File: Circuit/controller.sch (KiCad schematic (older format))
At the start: 13 parts, among them SW2 ROTARY_ENCODER_SWITCH, SW4 A, SW6 B, U4 JOYSTICK_W_BUTTON

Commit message: Rotated joystick to fit better.  X and Y are swapped.
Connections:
- net JOY_X: now also U4.Y2 (Y_WIPER); no longer U4.X2 (X_WIPER)
- net JOY_Y: now also U4.X2 (X_WIPER); no longer U4.Y2 (Y_WIPER)
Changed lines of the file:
@@
 Text HLabel 1000 850  2    60   Input ~ 0
 JOY_BUTTON
+Text HLabel 2500 1450 2    60   Input ~ 0
+JOY_X
 Text HLabel 2100 900  2    60   Input ~ 0
-JOY_X
-Text HLabel 2500 1450 2    60   Input ~ 0
 JOY_Y
 Wire Wire Line

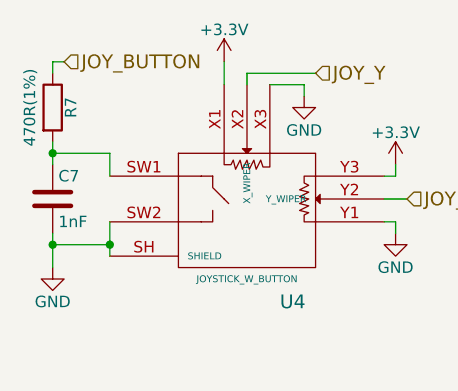
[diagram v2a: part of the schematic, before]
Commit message: More BOM - passives mostly.
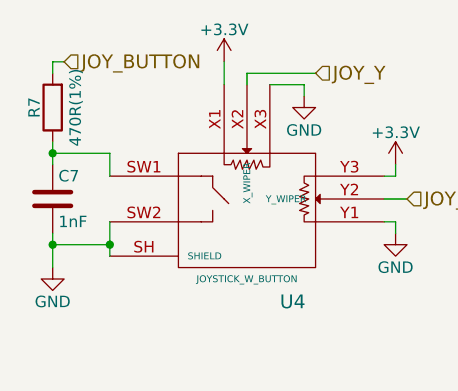
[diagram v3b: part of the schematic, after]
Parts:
- R10, R11, R8: Digikey PN (none) -> 311-10KGRCT-ND; Link (none) -> http://www.digikey.com.au/product-detail/en/yageo/RC0603JR-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; Manufacturer PN (none) -> RC0603JR-0710KL; Unit Cost (none) -> 0.10
- R12, R14, R7: Digikey PN (none) -> 311-470HRCT-ND; Link (none) -> http://www.digikey.com.au/product-detail/en/yageo/RC0603FR-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; Manufacturer PN (none) -> RC0603FR-07470RL; Unit Cost (none) -> 0.10
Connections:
- net JOY_BUTTON: now also R7.2; no longer R7.1
- net at C7.1, U4.SW1: now also R7.1; no longer R7.2
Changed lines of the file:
@@
-$EndComp
-$Comp
-L R R7
-U 1 1 58137E6F
-P 950 1050
-F 0 "R7" V 1030 1050 50  0000 C CNN
-F 1 "470R(1%)" V 850 1050 50  0000 C CNN
-F 2 "Resistors_SMD:R_0603_HandSoldering" V 880 1050 50  0001 C CNN
-F 3 "" H 950 1050 50  0000 C CNN
-	1    950  1050
-	1    0    0    -1
 $EndComp
 $Comp
@@
 $EndComp
 $Comp
-L R R12
-U 1 1 5813BFFC
-P 5450 1000
-F 0 "R12" V 5530 1000 50  0000 C CNN
-F 1 "470R(1%)" V 5350 1000 50  0000 C CNN
-F 2 "Resistors_SMD:R_0603_HandSoldering" V 5380 1000 50  0001 C CNN
-F 3 "" H 5450 1000 50  0000 C CNN
-	1    5450 1000
-	0    1    1    0
-$EndComp
-$Comp
 L GND #PWR053
 U 1 1 5813C06B
@@
 $EndComp
 $Comp
-L R R14
-U 1 1 5813C2E3
-P 5450 2050
-F 0 "R14" V 5530 2050 50  0000 C CNN
-F 1 "470R(1%)" V 5350 2050 50  0000 C CNN
-F 2 "Resistors_SMD:R_0603_HandSoldering" V 5380 2050 50  0001 C CNN
-F 3 "" H 5450 2050 50  0000 C CNN
-	1    5450 2050
-	0    1    1    0
-$EndComp
-$Comp
 L GND #PWR054
 U 1 1 5813C2E9
@@
 	1    0    0    -1
 $EndComp
-$Comp
-L R R10
-U 1 1 58141771
-P 1500 3550
-F 0 "R10" V 1580 3550 50  0000 C CNN
-F 1 "10K" V 1400 3550 50  0000 C CNN
-F 2 "Resistors_SMD:R_0603_HandSoldering" V 1430 3550 50  0001 C CNN
-F 3 "" H 1500 3550 50  0000 C CNN
-	1    1500 3550
-	0    1    1    0
-$EndComp
 Wire Wire Line
 	1550 3950 1550 3750
@@
 	2800 3850 2500 3850
 $Comp
-L R R11
-U 1 1 58141984
-P 2750 3650
-F 0 "R11" V 2830 3650 50  0000 C CNN
-F 1 "10K" V 2650 3650 50  0000 C CNN
-F 2 "Resistors_SMD:R_0603_HandSoldering" V 2680 3650 50  0001 C CNN
-F 3 "" H 2750 3650 50  0000 C CNN
-	1    2750 3650
-	0    1    1    0
-$EndComp
-$Comp
 L +3.3V #PWR057
 U 1 1 58141A8C
@@
 	2550 3300 2550 3650
 $Comp
-L R R8
-U 1 1 58141E89
-P 1500 3200
-F 0 "R8" V 1580 3200 50  0000 C CNN
-F 1 "10K" V 1400 3200 50  0000 C CNN
-F 2 "Resistors_SMD:R_0603_HandSoldering" V 1430 3200 50  0001 C CNN
-F 3 "" H 1500 3200 50  0000 C CNN
-	1    1500 3200
-	0    1    1    0
-$EndComp
-$Comp
 L +3.3V #PWR058
 U 1 1 58141FF1
@@
 Connection ~ 1750 3550
 Connection ~ 1850 3200
+$Comp
+L R R8
+U 1 1 58222193
+P 1500 3200
+F 0 "R8" V 1580 3200 50  0000 C CNN
+F 1 "10K" V 1400 3200 50  0000 C CNN
+F 2 "Resistors_SMD:R_0603_HandSoldering" V 1430 3200 50  0001 C CNN
+F 3 "" H 1500 3200 50  0000 C CNN
+F 4 "311-10KGRCT-ND" V 1500 3200 60  0001 C CNN "Digikey PN"
+F 5 "http://www.digikey.com.au/product-detail/en/yageo/RC0603JR-0710KL/311-10KGRCT-ND/729647" V 1500 3200 60  0001 C CNN "Link"
+F 6 "RC0603JR-0710KL" V 1500 3200 60  0001 C CNN "Manufacturer PN"
+F 7 "0.10" V 1500 3200 60  0001 C CNN "Unit Cost"
+	1    1500 3200
+	0    1    1    0
+$EndComp
+$Comp
+L R R10
+U 1 1 582222D7
+P 1500 3550
+F 0 "R10" V 1580 3550 50  0000 C CNN
+F 1 "10K" V 1400 3550 50  0000 C CNN
+F 2 "Resistors_SMD:R_0603_HandSoldering" V 1430 3550 50  0001 C CNN
+F 3 "" H 1500 3550 50  0000 C CNN
+F 4 "311-10KGRCT-ND" V 1500 3550 60  0001 C CNN "Digikey PN"
+F 5 "http://www.digikey.com.au/product-detail/en/yageo/RC0603JR-0710KL/311-10KGRCT-ND/729647" V 1500 3550 60  0001 C CNN "Link"
+F 6 "RC0603JR-0710KL" V 1500 3550 60  0001 C CNN "Manufacturer PN"
+F 7 "0.10" V 1500 3550 60  0001 C CNN "Unit Cost"
+	1    1500 3550
+	0    1    1    0
+$EndComp
+$Comp
+L R R11
+U 1 1 58222368
+P 2750 3650
+F 0 "R11" V 2830 3650 50  0000 C CNN
+F 1 "10K" V 2650 3650 50  0000 C CNN
+F 2 "Resistors_SMD:R_0603_HandSoldering" V 2680 3650 50  0001 C CNN
+F 3 "" H 2750 3650 50  0000 C CNN
+F 4 "311-10KGRCT-ND" V 2750 3650 60  0001 C CNN "Digikey PN"
+F 5 "http://www.digikey.com.au/product-detail/en/yageo/RC0603JR-0710KL/311-10KGRCT-ND/729647" V 2750 3650 60  0001 C CNN "Link"
+F 6 "RC0603JR-0710KL" V 2750 3650 60  0001 C CNN "Manufacturer PN"
+F 7 "0.10" V 2750 3650 60  0001 C CNN "Unit Cost"
+	1    2750 3650
+	0    1    1    0
+$EndComp
+$Comp
+L R R12
+U 1 1 58224979
+P 5450 1000
+F 0 "R12" V 5530 1000 50  0000 C CNN
+F 1 "470R(1%)" V 5350 1000 50  0000 C CNN
+F 2 "Resistors_SMD:R_0603_HandSoldering" V 5380 1000 50  0001 C CNN
+F 3 "" H 5450 1000 50  0000 C CNN
+F 4 "311-470HRCT-ND" V 5450 1000 60  0001 C CNN "Digikey PN"
+F 5 "http://www.digikey.com.au/product-detail/en/yageo/RC0603FR-07470RL/311-470HRCT-ND/730203" V 5450 1000 60  0001 C CNN "Link"
+F 6 "RC0603FR-07470RL" V 5450 1000 60  0001 C CNN "Manufacturer PN"
+F 7 "0.10" V 5450 1000 60  0001 C CNN "Unit Cost"
+	1    5450 1000
+	0    1    1    0
+$EndComp
+$Comp
+L R R14
+U 1 1 58224A61
+P 5450 2050
+F 0 "R14" V 5530 2050 50  0000 C CNN
+F 1 "470R(1%)" V 5350 2050 50  0000 C CNN
+F 2 "Resistors_SMD:R_0603_HandSoldering" V 5380 2050 50  0001 C CNN
+F 3 "" H 5450 2050 50  0000 C CNN
+F 4 "311-470HRCT-ND" V 5450 2050 60  0001 C CNN "Digikey PN"
+F 5 "http://www.digikey.com.au/product-detail/en/yageo/RC0603FR-07470RL/311-470HRCT-ND/730203" V 5450 2050 60  0001 C CNN "Link"
+F 6 "RC0603FR-07470RL" V 5450 2050 60  0001 C CNN "Manufacturer PN"
+F 7 "0.10" V 5450 2050 60  0001 C CNN "Unit Cost"
+	1    5450 2050
+	0    1    1    0
+$EndComp
+$Comp
+L R R7
+U 1 1 58224EE1
+P 950 1050
+F 0 "R7" V 1030 1050 50  0000 C CNN
+F 1 "470R(1%)" V 850 1050 50  0000 C CNN
+F 2 "Resistors_SMD:R_0603_HandSoldering" V 880 1050 50  0001 C CNN
+F 3 "" H 950 1050 50  0000 C CNN
+F 4 "311-470HRCT-ND" V 950 1050 60  0001 C CNN "Digikey PN"
+F 5 "http://www.digikey.com.au/product-detail/en/yageo/RC0603FR-07470RL/311-470HRCT-ND/730203" V 950 1050 60  0001 C CNN "Link"
+F 6 "RC0603FR-07470RL" V 950 1050 60  0001 C CNN "Manufacturer PN"
+F 7 "0.10" V 950 1050 60  0001 C CNN "Unit Cost"
+	1    950  1050
+	-1   0    0    1
+$EndComp
 $EndSCHEMATC

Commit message: BOM. Some passives & transistors. Nearly done.
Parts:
- C7, C8, C9: Digikey PN (none) -> 490-3184-1-ND; Link (none) -> http://www.digikey.com.au/product-detail/en/murata-electron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; Manufacturer PN (none) -> GRM033R71E102KA01D; Unit Cost (none) -> 0.10
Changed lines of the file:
@@
-$EndComp
-$Comp
-L C C7
-U 1 1 58137EF2
-P 950 1450
-F 0 "C7" H 975 1550 50  0000 L CNN
-F 1 "1nF" H 975 1350 50  0000 L CNN
-F 2 "Capacitors_SMD:C_0603_HandSoldering" H 988 1300 50  0001 C CNN
-F 3 "" H 950 1450 50  0000 C CNN
-	1    950  1450
-	1    0    0    -1
 $EndComp
 $Comp
@@
 F 2 "Capacitors_SMD:C_0603_HandSoldering" H 5238 1150 50  0001 C CNN
 F 3 "" H 5200 1300 50  0000 C CNN
+F 4 "490-3184-1-ND" H 5200 1300 60  0001 C CNN "Digikey PN"
+F 5 "http://www.digikey.com.au/product-detail/en/murata-electronics-north-america/GRM033R71E102KA01D/490-3184-1-ND/702725" H 5200 1300 60  0001 C CNN "Link"
+F 6 "GRM033R71E102KA01D" H 5200 1300 60  0001 C CNN "Manufacturer PN"
+F 7 "0.10" H 5200 1300 60  0001 C CNN "Unit Cost"
 	1    5200 1300
 	1    0    0    -1
@@
 	1    4950 2350
 	0    -1   -1   0
-$EndComp
-$Comp
-L C C9
-U 1 1 5813C2DD
-P 5200 2350
-F 0 "C9" H 5225 2450 50  0000 L CNN
-F 1 "1nF" H 5225 2250 50  0000 L CNN
-F 2 "Capacitors_SMD:C_0603_HandSoldering" H 5238 2200 50  0001 C CNN
-F 3 "" H 5200 2350 50  0000 C CNN
-	1    5200 2350
-	1    0    0    -1
 $EndComp
 $Comp
@@
 	-1   0    0    1
 $EndComp
+$Comp
+L C C9
+U 1 1 58230857
+P 5200 2350
+F 0 "C9" H 5225 2450 50  0000 L CNN
+F 1 "1nF" H 5225 2250 50  0000 L CNN
+F 2 "Capacitors_SMD:C_0603_HandSoldering" H 5238 2200 50  0001 C CNN
+F 3 "" H 5200 2350 50  0000 C CNN
+F 4 "490-3184-1-ND" H 5200 2350 60  0001 C CNN "Digikey PN"
+F 5 "http://www.digikey.com.au/product-detail/en/murata-electronics-north-america/GRM033R71E102KA01D/490-3184-1-ND/702725" H 5200 2350 60  0001 C CNN "Link"
+F 6 "GRM033R71E102KA01D" H 5200 2350 60  0001 C CNN "Manufacturer PN"
+F 7 "0.10" H 5200 2350 60  0001 C CNN "Unit Cost"
+	1    5200 2350
+	1    0    0    -1
+$EndComp
+$Comp
+L C C7
+U 1 1 582308E6
+P 950 1450
+F 0 "C7" H 975 1550 50  0000 L CNN
+F 1 "1nF" H 975 1350 50  0000 L CNN
+F 2 "Capacitors_SMD:C_0603_HandSoldering" H 988 1300 50  0001 C CNN
+F 3 "" H 950 1450 50  0000 C CNN
+F 4 "490-3184-1-ND" H 950 1450 60  0001 C CNN "Digikey PN"
+F 5 "http://www.digikey.com.au/product-detail/en/murata-electronics-north-america/GRM033R71E102KA01D/490-3184-1-ND/702725" H 950 1450 60  0001 C CNN "Link"
+F 6 "GRM033R71E102KA01D" H 950 1450 60  0001 C CNN "Manufacturer PN"
+F 7 "0.10" H 950 1450 60  0001 C CNN "Unit Cost"
+	1    950  1450
+	1    0    0    -1
+$EndComp
 $EndSCHEMATC
